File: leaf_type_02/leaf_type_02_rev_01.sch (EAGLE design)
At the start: 18 parts, among them J1 TC_2050_IDC_NL_TOP, J2 CONN_5X2_0P05_IN_SMT, J4 CONN_4X1_JST_PA, J5 CONN_4X1_JST_PA, U1 RS485_XCVR_SN65HVD178X

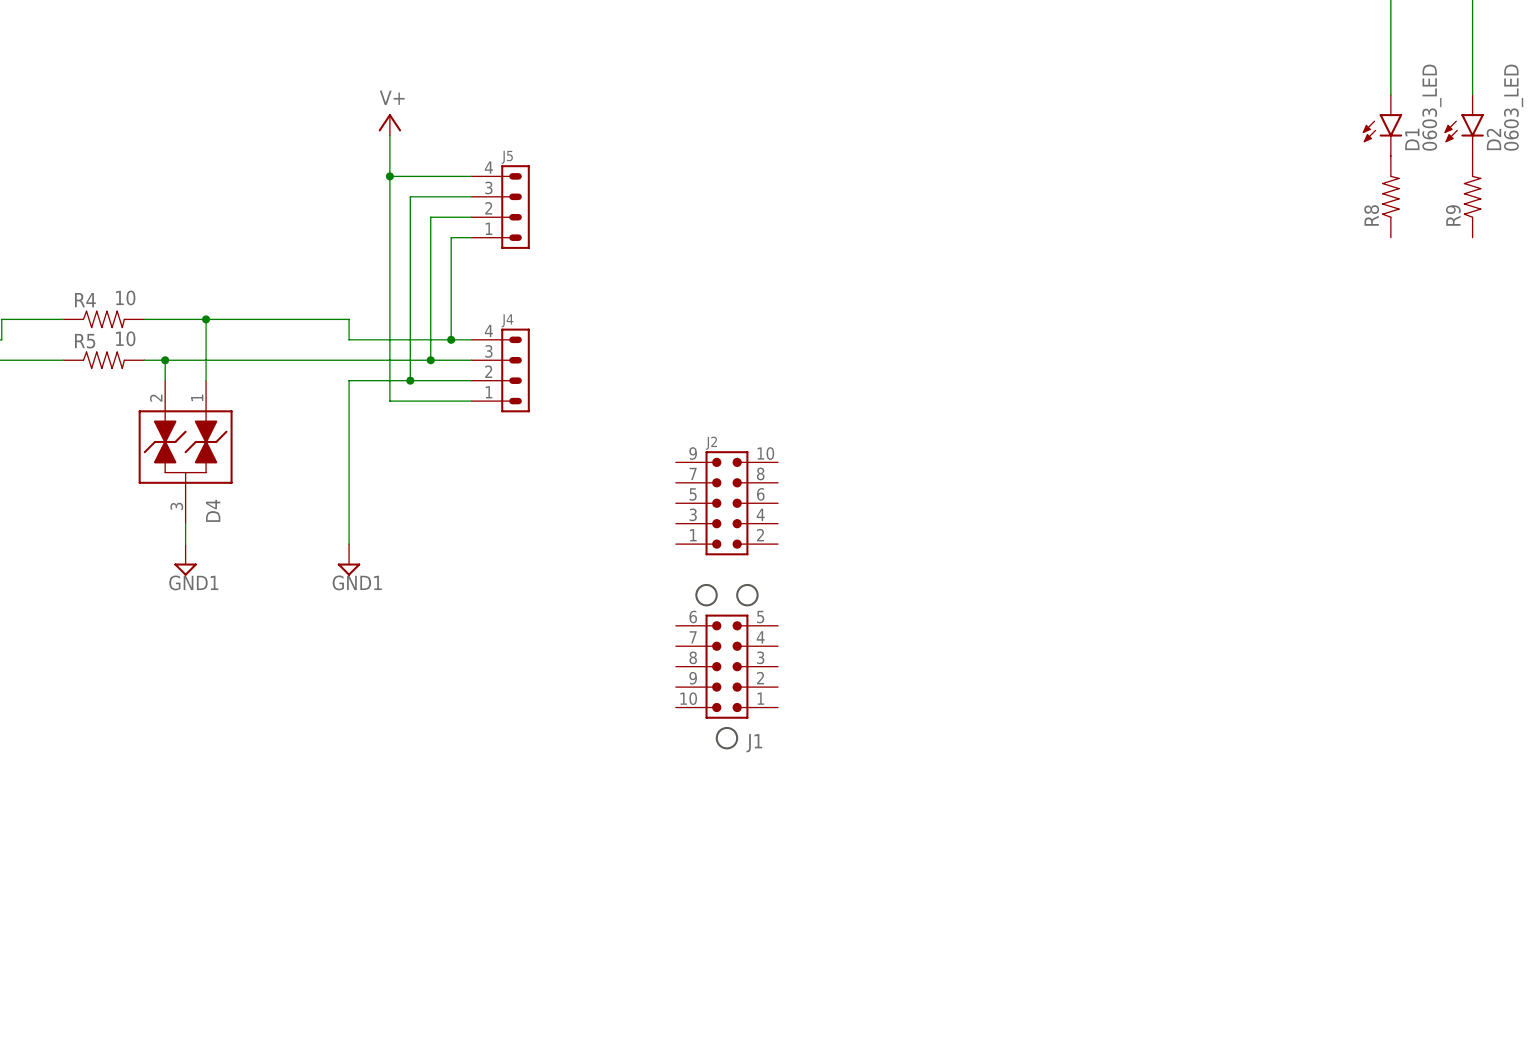
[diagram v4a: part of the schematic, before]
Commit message: stm32 part update
added stm32l031G6U6 part and added footprints for qfn 28, 32 & tfqp 32
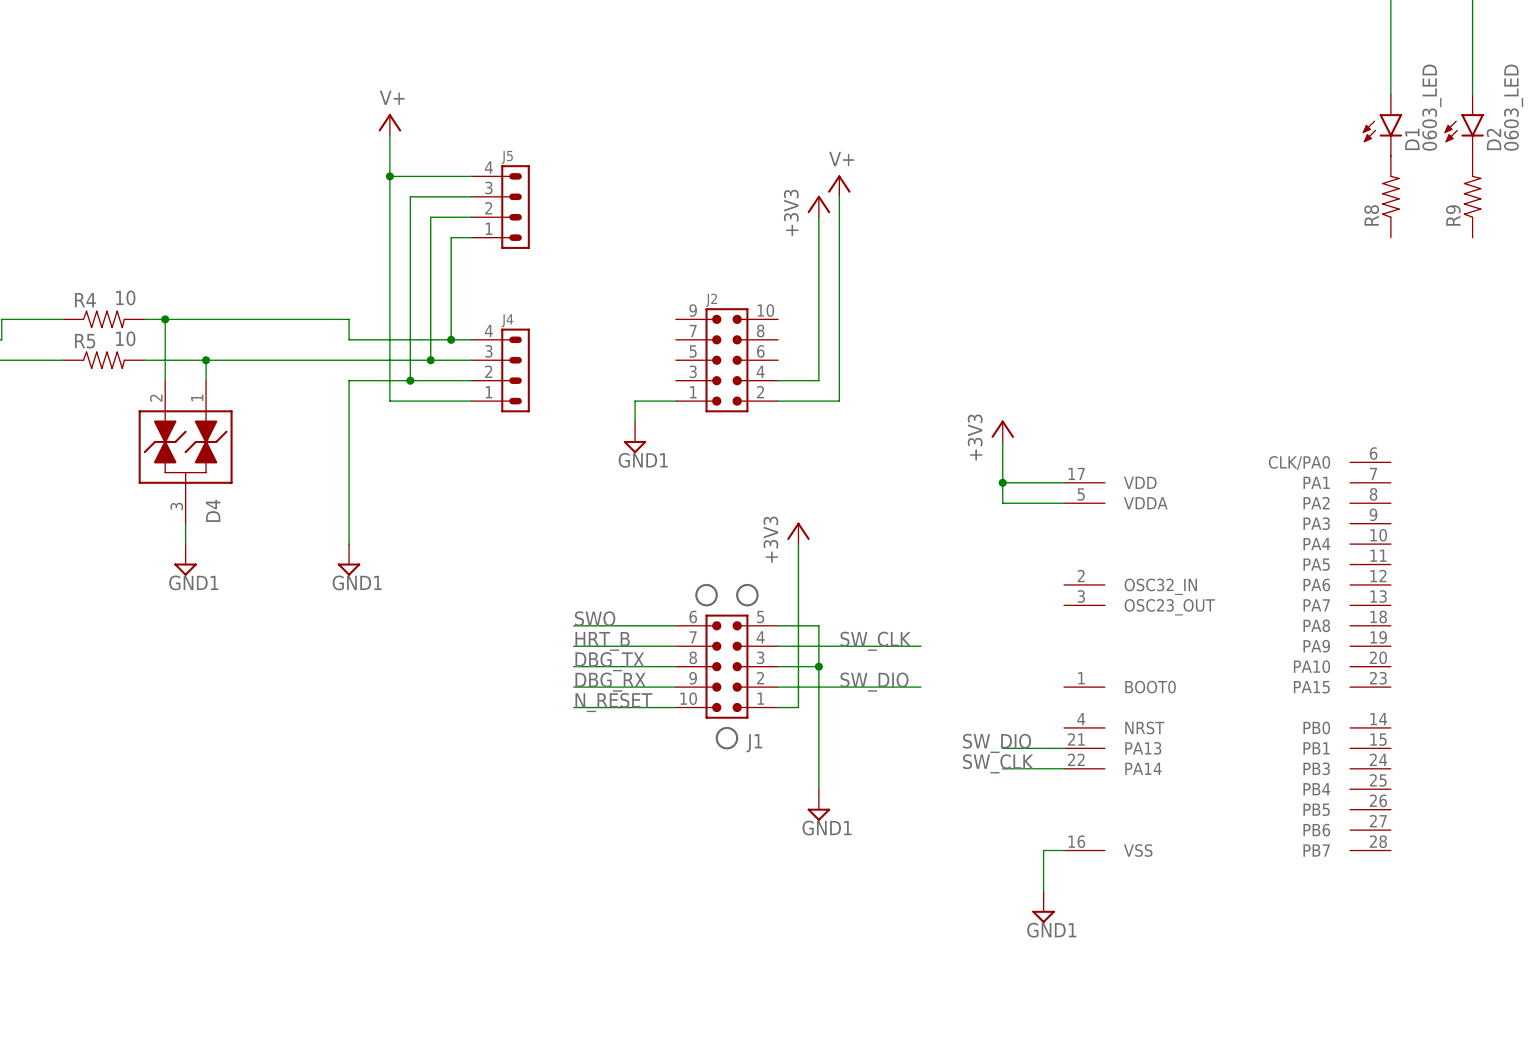
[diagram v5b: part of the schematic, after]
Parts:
- added U2: STM32L031G6U6, leaf:STM32L031G6U6
- R7, R8, R9: device stepOSP:0402_RES -> stepOSP:0603_RES
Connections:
- new net DBG_RX: J1.9
- new net DBG_TX: J1.8
- new net HRT_B: J1.7
- new net N_RESET: J1.10
- new net SWO: J1.6
- new net SW_CLK: J1.4, U2.PA14
- new net SW_DIO: J1.2, U2.PA13
- net +3V3: now also J1.1, J2.4, U2.VDD, U2.VDDA
- net GND1: now also J1.3, J1.5, J2.1, U2.VSS
- net N$1: now also D4.2; no longer D4.1
- net N$7: now also D4.1; no longer D4.2
- net V+: now also J2.2
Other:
- moved on the sheet: J2
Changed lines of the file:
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@@
 <?xml version="1.0" encoding="utf-8"?>
 <!DOCTYPE eagle SYSTEM "eagle.dtd">
-<eagle version="7.6.0">
+<eagle version="7.3.0">
 <drawing>
 <settings>
@@
 <part name="R4" library="stepOSP" deviceset="0603_RES" device="" value="10"/>
 <part name="R5" library="stepOSP" deviceset="0603_RES" device="" value="10"/>
-<part name="R7" library="stepOSP" deviceset="0402_RES" device="" value="3.3k"/>
+<part name="R7" library="stepOSP" deviceset="0603_RES" device="" value="3.3k"/>
 <part name="+3V2" library="supply1" deviceset="+3V3" device=""/>
 <part name="D4" library="leaf" deviceset="TVS_SOT-23" device=""/>
@@
 <part name="D1" library="stepOSP" deviceset="0603_LED" device=""/>
 <part name="D2" library="stepOSP" deviceset="0603_LED" device=""/>
-<part name="R8" library="stepOSP" deviceset="0402_RES" device=""/>
-<part name="R9" library="stepOSP" deviceset="0402_RES" device=""/>
+<part name="R8" library="stepOSP" deviceset="0603_RES" device=""/>
+<part name="R9" library="stepOSP" deviceset="0603_RES" device=""/>
 <part name="U$2" library="stepOSP" deviceset="TPS709XX" device=""/>
 <part name="C2" library="stepOSP" deviceset="0603_CAP" device=""/>
@@
 <part name="J4" library="leaf" deviceset="CONN_4X1_JST_PA" device=""/>
 <part name="J5" library="leaf" deviceset="CONN_4X1_JST_PA" device=""/>
+<part name="SUPPLY6" library="supply2" deviceset="GND1" device=""/>
+<part name="+3V3" library="supply1" deviceset="+3V3" device=""/>
+<part name="SUPPLY4" library="supply2" deviceset="GND1" device=""/>
+<part name="SUPPLY7" library="supply2" deviceset="V+" device=""/>
+<part name="+3V6" library="supply1" deviceset="+3V3" device=""/>
+<part name="U2" library="leaf" deviceset="STM32L031G6U6" device=""/>
+<part name="SUPPLY10" library="supply2" deviceset="GND1" device=""/>
+<part name="+3V7" library="supply1" deviceset="+3V3" device=""/>
 </parts>
 <sheets>
@@
 <instance part="R1" gate="G$1" x="101.6" y="165.1" rot="R90"/>
 <instance part="J1" gate="G$1" x="241.3" y="109.22"/>
-<instance part="J2" gate="G$1" x="241.3" y="129.54"/>
+<instance part="J2" gate="G$1" x="241.3" y="147.32"/>
 <instance part="J4" gate="G$1" x="213.36" y="147.32"/>
 <instance part="J5" gate="G$1" x="213.36" y="167.64"/>
+<instance part="SUPPLY6" gate="G$1" x="251.46" y="96.52"/>
+<instance part="+3V3" gate="G$1" x="248.92" y="132.08"/>
+<instance part="SUPPLY4" gate="G$1" x="228.6" y="142.24"/>
+<instance part="SUPPLY7" gate="1" x="254" y="175.26"/>
+<instance part="+3V6" gate="G$1" x="251.46" y="172.72"/>
+<instance part="U2" gate="G$1" x="299.72" y="132.08"/>
+<instance part="SUPPLY10" gate="G$1" x="279.4" y="83.82"/>
+<instance part="+3V7" gate="G$1" x="274.32" y="144.78"/>
 </instances>
 <busses>
@@
 <wire x1="332.74" y1="205.74" x2="332.74" y2="185.42" width="0.1524" layer="91"/>
 </segment>
+<segment>
+<pinref part="J1" gate="G$1" pin="1"/>
+<wire x1="246.38" y1="109.22" x2="248.92" y2="109.22" width="0.1524" layer="91"/>
+<wire x1="248.92" y1="109.22" x2="248.92" y2="129.54" width="0.1524" layer="91"/>
+<pinref part="+3V3" gate="G$1" pin="+3V3"/>
+</segment>
+<segment>
+<pinref part="J2" gate="G$1" pin="4"/>
+<wire x1="246.38" y1="149.86" x2="251.46" y2="149.86" width="0.1524" layer="91"/>
+<wire x1="251.46" y1="149.86" x2="251.46" y2="170.18" width="0.1524" layer="91"/>
+<pinref part="+3V6" gate="G$1" pin="+3V3"/>
+</segment>
+<segment>
+<pinref part="U2" gate="G$1" pin="VDD"/>
+<pinref part="+3V7" gate="G$1" pin="+3V3"/>
+<wire x1="281.94" y1="137.16" x2="274.32" y2="137.16" width="0.1524" layer="91"/>
+<wire x1="274.32" y1="137.16" x2="274.32" y2="142.24" width="0.1524" layer="91"/>
+<pinref part="U2" gate="G$1" pin="VDDA"/>
+<wire x1="281.94" y1="134.62" x2="274.32" y2="134.62" width="0.1524" layer="91"/>
+<wire x1="274.32" y1="134.62" x2="274.32" y2="137.16" width="0.1524" layer="91"/>
+<junction x="274.32" y="137.16"/>
+</segment>
 </net>
 <net name="V+" class="0">
@@
 <wire x1="208.28" y1="175.26" x2="198.12" y2="175.26" width="0.1524" layer="91"/>
 <junction x="198.12" y="175.26"/>
+</segment>
+<segment>
+<pinref part="SUPPLY7" gate="1" pin="V+"/>
+<pinref part="J2" gate="G$1" pin="2"/>
+<wire x1="246.38" y1="147.32" x2="254" y2="147.32" width="0.1524" layer="91"/>
+<wire x1="254" y1="147.32" x2="254" y2="172.72" width="0.1524" layer="91"/>
 </segment>
 </net>
@@
 <wire x1="101.6" y1="129.54" x2="101.6" y2="132.08" width="0.1524" layer="91"/>
 </segment>
+<segment>
+<pinref part="J1" gate="G$1" pin="3"/>
+<wire x1="246.38" y1="114.3" x2="251.46" y2="114.3" width="0.1524" layer="91"/>
+<wire x1="251.46" y1="114.3" x2="251.46" y2="99.06" width="0.1524" layer="91"/>
+<pinref part="SUPPLY6" gate="G$1" pin="GND1"/>
+<pinref part="J1" gate="G$1" pin="5"/>
+<wire x1="246.38" y1="119.38" x2="251.46" y2="119.38" width="0.1524" layer="91"/>
+<wire x1="251.46" y1="119.38" x2="251.46" y2="114.3" width="0.1524" layer="91"/>
+<junction x="251.46" y="114.3"/>
+</segment>
+<segment>
+<pinref part="J2" gate="G$1" pin="1"/>
+<pinref part="SUPPLY4" gate="G$1" pin="GND1"/>
+<wire x1="233.68" y1="147.32" x2="228.6" y2="147.32" width="0.1524" layer="91"/>
+<wire x1="228.6" y1="147.32" x2="228.6" y2="144.78" width="0.1524" layer="91"/>
+</segment>
+<segment>
+<pinref part="U2" gate="G$1" pin="VSS"/>
+<pinref part="SUPPLY10" gate="G$1" pin="GND1"/>
+<wire x1="281.94" y1="91.44" x2="279.4" y2="91.44" width="0.1524" layer="91"/>
+<wire x1="279.4" y1="91.44" x2="279.4" y2="86.36" width="0.1524" layer="91"/>
+</segment>
 </net>
 <net name="N$7" class="0">
 <segment>
 <pinref part="R5" gate="G$1" pin="2"/>
-<wire x1="170.18" y1="152.4" x2="167.64" y2="152.4" width="0.1524" layer="91"/>
-<pinref part="D4" gate="G$1" pin="2"/>
-<wire x1="170.18" y1="149.86" x2="170.18" y2="152.4" width="0.1524" layer="91"/>
-<junction x="170.18" y="152.4"/>
-<wire x1="203.2" y1="152.4" x2="170.18" y2="152.4" width="0.1524" layer="91"/>
+<wire x1="203.2" y1="152.4" x2="175.26" y2="152.4" width="0.1524" layer="91"/>
+<wire x1="175.26" y1="152.4" x2="167.64" y2="152.4" width="0.1524" layer="91"/>
 <wire x1="203.2" y1="152.4" x2="203.2" y2="170.18" width="0.1524" layer="91"/>
 <pinref part="J4" gate="G$1" pin="3"/>
@@
 <pinref part="J5" gate="G$1" pin="2"/>
 <wire x1="208.28" y1="170.18" x2="203.2" y2="170.18" width="0.1524" layer="91"/>
+<pinref part="D4" gate="G$1" pin="1"/>
+<wire x1="175.26" y1="152.4" x2="175.26" y2="149.86" width="0.1524" layer="91"/>
+<junction x="175.26" y="152.4"/>
 </segment>
 </net>
@@
 <segment>
 <pinref part="R4" gate="G$1" pin="2"/>
-<wire x1="167.64" y1="157.48" x2="175.26" y2="157.48" width="0.1524" layer="91"/>
-<wire x1="175.26" y1="157.48" x2="193.04" y2="157.48" width="0.1524" layer="91"/>
+<wire x1="167.64" y1="157.48" x2="170.18" y2="157.48" width="0.1524" layer="91"/>
+<wire x1="170.18" y1="157.48" x2="193.04" y2="157.48" width="0.1524" layer="91"/>
 <wire x1="193.04" y1="154.94" x2="193.04" y2="157.48" width="0.1524" layer="91"/>
-<pinref part="D4" gate="G$1" pin="1"/>
-<wire x1="175.26" y1="149.86" x2="175.26" y2="157.48" width="0.1524" layer="91"/>
-<junction x="175.26" y="157.48"/>
 <wire x1="205.74" y1="154.94" x2="193.04" y2="154.94" width="0.1524" layer="91"/>
 <wire x1="205.74" y1="154.94" x2="205.74" y2="167.64" width="0.1524" layer="91"/>
@@
 <pinref part="J5" gate="G$1" pin="1"/>
 <wire x1="208.28" y1="167.64" x2="205.74" y2="167.64" width="0.1524" layer="91"/>
+<pinref part="D4" gate="G$1" pin="2"/>
+<wire x1="170.18" y1="157.48" x2="170.18" y2="149.86" width="0.1524" layer="91"/>
+<junction x="170.18" y="157.48"/>
 </segment>
 </net>
@@
 </segment>
 </net>
+<net name="SW_DIO" class="0">
+<segment>
+<pinref part="J1" gate="G$1" pin="2"/>
+<wire x1="246.38" y1="111.76" x2="264.16" y2="111.76" width="0.1524" layer="91"/>
+<label x="254" y="111.76" size="1.778" layer="95"/>
+</segment>
+<segment>
+<pinref part="U2" gate="G$1" pin="PA13"/>
+<wire x1="281.94" y1="104.14" x2="274.32" y2="104.14" width="0.1524" layer="91"/>
+<label x="269.24" y="104.14" size="1.778" layer="95"/>
+</segment>
+</net>
+<net name="N_RESET" class="0">
+<segment>
+<pinref part="J1" gate="G$1" pin="10"/>
+<wire x1="233.68" y1="109.22" x2="220.98" y2="109.22" width="0.1524" layer="91"/>
+<label x="220.98" y="109.22" size="1.778" layer="95"/>
+</segment>
+</net>
+<net name="DBG_TX" class="0">
+<segment>
+<pinref part="J1" gate="G$1" pin="8"/>
+<wire x1="233.68" y1="114.3" x2="220.98" y2="114.3" width="0.1524" layer="91"/>
+<label x="220.98" y="114.3" size="1.778" layer="95"/>
+</segment>
+</net>
+<net name="SWO" class="0">
+<segment>
+<pinref part="J1" gate="G$1" pin="6"/>
+<wire x1="233.68" y1="119.38" x2="220.98" y2="119.38" width="0.1524" layer="91"/>
+<label x="220.98" y="119.38" size="1.778" layer="95"/>
+</segment>
+</net>
+<net name="SW_CLK" class="0">
+<segment>
+<pinref part="J1" gate="G$1" pin="4"/>
+<wire x1="246.38" y1="116.84" x2="264.16" y2="116.84" width="0.1524" layer="91"/>
+<label x="254" y="116.84" size="1.778" layer="95"/>
+</segment>
+<segment>
+<pinref part="U2" gate="G$1" pin="PA14"/>
+<wire x1="281.94" y1="101.6" x2="274.32" y2="101.6" width="0.1524" layer="91"/>
+<label x="269.24" y="101.6" size="1.778" layer="95"/>
+</segment>
+</net>
+<net name="HRT_B" class="0">
+<segment>
+<pinref part="J1" gate="G$1" pin="7"/>
+<wire x1="233.68" y1="116.84" x2="220.98" y2="116.84" width="0.1524" layer="91"/>
+<label x="220.98" y="116.84" size="1.778" layer="95"/>
+</segment>
+</net>
+<net name="DBG_RX" class="0">
+<segment>
+<pinref part="J1" gate="G$1" pin="9"/>
+<wire x1="233.68" y1="111.76" x2="220.98" y2="111.76" width="0.1524" layer="91"/>
+<label x="220.98" y="111.76" size="1.778" layer="95"/>
+</segment>
+</net>
